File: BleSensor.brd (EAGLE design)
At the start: 31.7 x 37.3 mm, 13 parts, among them T1 BPW85C, U1 PIC12F1572/P

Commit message: Added sensors
Added sensors
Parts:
- added U2: LMT84-TO-92LP, Temperature sensor:TO92-LP
- moved T1 45.0 mm to (15.2, 27.3)
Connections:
- new net N$13: T1.A
- net GND: now also U2.2
- net RA3: now also U2.1
- net RA4: now also U2.3
- net RA5: no longer T1.A
- net VDD: no longer T1.K, U1.1
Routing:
- net VDD: track 80.4 -> 69.2 mm
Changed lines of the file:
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@@
 <?xml version="1.0" encoding="utf-8"?>
 <!DOCTYPE eagle SYSTEM "eagle.dtd">
-<eagle version="7.5.0">
+<eagle version="8.4.0">
 <drawing>
 <settings>
 <setting alwaysvectorfont="no"/>
+<setting keepoldvectorfont="yes"/>
 <setting verticaltext="up"/>
 </settings>
@@
 <layer number="51" name="tDocu" color="7" fill="1" visible="yes" active="yes"/>
 <layer number="52" name="bDocu" color="7" fill="1" visible="yes" active="yes"/>
+<layer number="88" name="SimResults" color="9" fill="1" visible="no" active="no"/>
+<layer number="89" name="SimProbes" color="9" fill="1" visible="no" active="no"/>
 <layer number="90" name="Modules" color="5" fill="1" visible="no" active="no"/>
 <layer number="91" name="Nets" color="2" fill="1" visible="no" active="no"/>
@@
 <param name="dpMaxLengthDifference" value="10mm"/>
 <param name="dpGapFactor" value="2.5"/>
-<param name="checkGrid" value="0"/>
-<param name="checkAngle" value="0"/>
 <param name="checkFont" value="1"/>
 <param name="checkRestrict" value="1"/>
+<param name="checkStop" value="0"/>
 <param name="useDiameter" value="13"/>
 <param name="maxErrors" value="50"/>
@@
 <element name="R2" library="resistor" package="M1206" value="47K" x="2.54" y="-3.81"/>
 <element name="R3" library="resistor" package="M1206" value="22K" x="2.54" y="-10.16"/>
-<element name="T1" library="Vishay_tsal4400_bpw85c" package="LED3MM" value="BPW85C" x="2.54" y="-15.875"/>
+<element name="T1" library="Vishay_tsal4400_bpw85c" package="LED3MM" value="BPW85C" x="15.24" y="27.305"/>
 <element name="C4" library="rcl" package="C1206" value="1nF" x="2.54" y="-21.59"/>
+<element name="U2" library="Temperature sensor" package="TO92-LP" value="LMT84-TO-92LP" x="3.175" y="-33.02"/>
 </elements>
 <signals>
@@
 <signal name="VDD">
 <contactref element="C1" pad="1"/>
-<contactref element="U1" pad="1"/>
 <contactref element="JP1" pad="10"/>
-<wire x1="3.81" y1="11.43" x2="12.7" y2="11.43" width="0.8128" layer="16"/>
 <contactref element="JP1" pad="9"/>
 <wire x1="3.81" y1="11.43" x2="3.81" y2="13.97" width="0.8128" layer="16"/>
@@
 <contactref element="C2" pad="1"/>
 <contactref element="C3" pad="1"/>
-<wire x1="12.7" y1="11.43" x2="12.7" y2="12.7" width="0.4064" layer="1"/>
 <wire x1="12.7" y1="12.7" x2="13.716" y2="13.716" width="0.4064" layer="1"/>
 <wire x1="13.716" y1="13.716" x2="15.11" y2="13.716" width="0.4064" layer="1"/>
@@
 <wire x1="16.51" y1="2.54" x2="16.51" y2="8.636" width="0.8128" layer="16"/>
 <wire x1="16.51" y1="8.636" x2="13.716" y2="11.43" width="0.8128" layer="16"/>
-<wire x1="13.716" y1="11.43" x2="12.7" y2="11.43" width="0.8128" layer="16"/>
 <wire x1="17.526" y1="1.524" x2="22.86" y2="1.524" width="0.8128" layer="16"/>
 <wire x1="22.86" y1="1.524" x2="24.13" y2="2.794" width="0.8128" layer="16"/>
@@
 <wire x1="23.876" y1="32.512" x2="21.458" y2="32.512" width="0.3048" layer="1"/>
 <wire x1="21.458" y1="32.512" x2="21.41" y2="32.56" width="0.4064" layer="1"/>
-<contactref element="T1" pad="K"/>
-<wire x1="3.81" y1="-15.875" x2="17.526" y2="1.524" width="0" layer="19" extent="16-16"/>
+<wire x1="13.716" y1="11.43" x2="12.7" y2="12.7" width="0" layer="19" extent="1-16"/>
+<wire x1="7.49" y1="11.43" x2="12.7" y2="12.7" width="0" layer="19" extent="1-1"/>
 </signal>
 <signal name="RA2">
@@
 <wire x1="22.86" y1="13.97" x2="25.4" y2="16.51" width="0.254" layer="1"/>
 <wire x1="25.4" y1="16.51" x2="26.67" y2="16.51" width="0.254" layer="1"/>
+<contactref element="U2" pad="3"/>
+<wire x1="12.7" y1="6.35" x2="4.445" y2="-31.75" width="0" layer="19" extent="1-1"/>
 </signal>
 <signal name="RA3">
@@
 <wire x1="4.064" y1="19.304" x2="3.81" y2="19.05" width="0.254" layer="1"/>
 <contactref element="R2" pad="2"/>
-<wire x1="17.526" y1="7.62" x2="4.826" y2="19.304" width="0" layer="19" extent="1-1"/>
-<wire x1="3.94" y1="-3.81" x2="12.7" y2="3.81" width="0" layer="19" extent="1-1"/>
+<contactref element="U2" pad="1"/>
+<wire x1="3.94" y1="-3.81" x2="1.905" y2="-31.75" width="0" layer="19" extent="1-1"/>
+<wire x1="12.7" y1="3.81" x2="3.94" y2="-3.81" width="0" layer="19" extent="1-1"/>
+<wire x1="4.826" y1="19.304" x2="17.526" y2="7.62" width="0" layer="19" extent="1-1"/>
 </signal>
 <signal name="RA5">
@@
 <wire x1="8.89" y1="10.16" x2="3.81" y2="8.89" width="0.254" layer="1"/>
 <wire x1="12.7" y1="8.89" x2="8.89" y2="10.16" width="0.254" layer="1"/>
-<contactref element="T1" pad="A"/>
 <contactref element="C4" pad="1"/>
-<wire x1="1.27" y1="-15.875" x2="1.14" y2="-21.59" width="0" layer="19" extent="1-1"/>
-<wire x1="8.89" y1="6.48" x2="1.27" y2="-15.875" width="0" layer="19" extent="1-1"/>
+<wire x1="8.89" y1="6.48" x2="1.14" y2="-21.59" width="0" layer="19" extent="1-1"/>
 <wire x1="8.89" y1="10.16" x2="8.89" y2="6.48" width="0" layer="19" extent="1-1"/>
 </signal>
@@
 <contactref element="R3" pad="1"/>
 <contactref element="C4" pad="2"/>
+<contactref element="U2" pad="2"/>
 <wire x1="15.872" y1="32.512" x2="21.41" y2="33.76" width="0" layer="19" extent="1-16"/>
 <wire x1="10.41" y1="33.76" x2="15.872" y2="32.512" width="0" layer="19" extent="1-16"/>
@@
 <wire x1="1.14" y1="-10.16" x2="8.89" y2="3.68" width="0" layer="19" extent="1-1"/>
 <wire x1="3.94" y1="-21.59" x2="1.14" y2="-10.16" width="0" layer="19" extent="1-1"/>
+<wire x1="3.175" y1="-31.75" x2="3.94" y2="-21.59" width="0" layer="19" extent="1-1"/>
 </signal>
 <signal name="BATT_MON">
@@
 <wire x1="3.94" y1="-10.16" x2="1.14" y2="-3.81" width="0" layer="19" extent="1-1"/>
 </signal>
+<signal name="N$13">
+<contactref element="T1" pad="A"/>
+</signal>
 </signals>

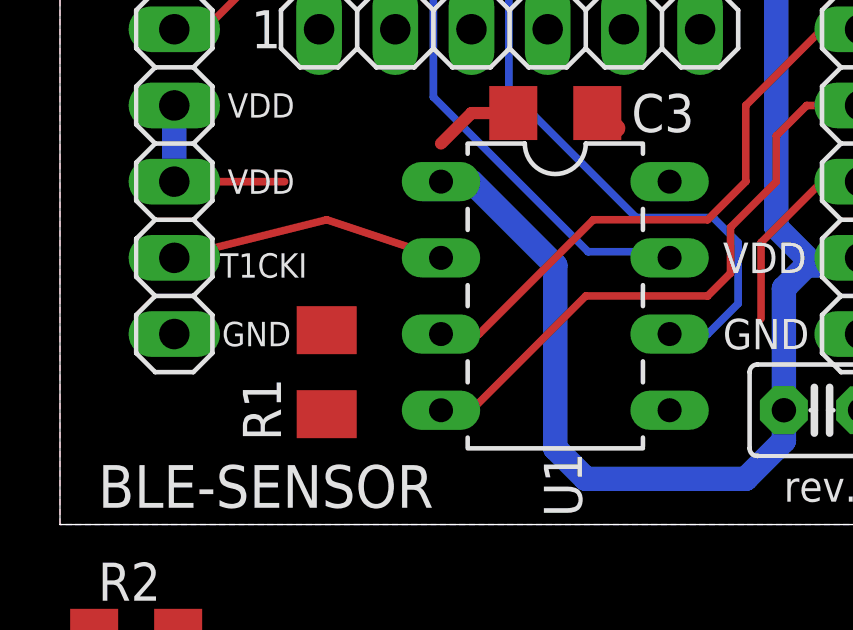
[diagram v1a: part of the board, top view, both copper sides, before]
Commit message: Fixed sensor inputs, added pdf Bitscope BLE Sensor pics
Fixed sensor inputs, added pdf Bitscope BLE Sensor pics
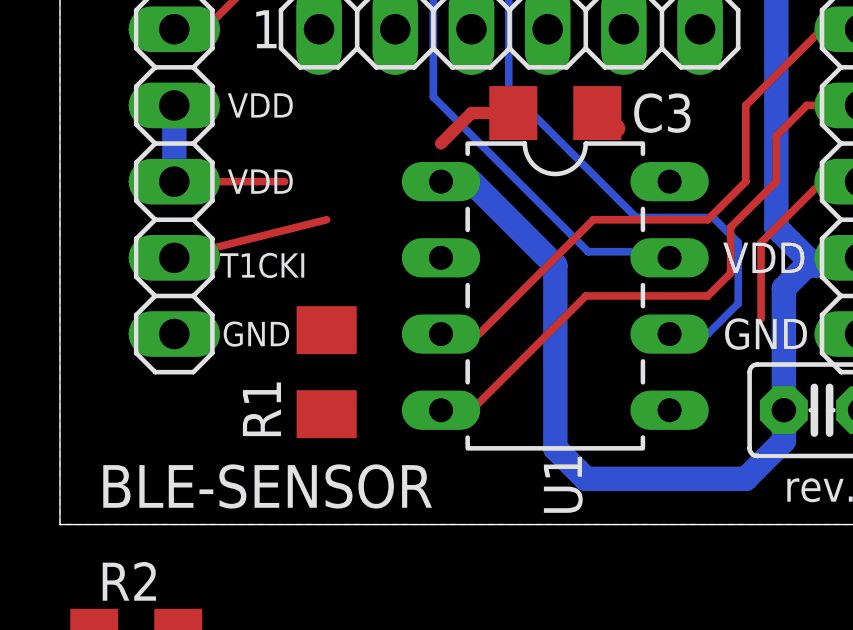
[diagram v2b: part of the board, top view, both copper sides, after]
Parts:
- C4: value 1nF -> 3n3
- R1: value 470K -> 100K
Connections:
- net N$13 renamed VE
- removed net N$12: JP1.4, U$1.P04
- new net TEMP: U2.3
- new net VC: T1.K
- new net WAKE-UP: R2.2, U2.1
- net BATT_MON: now also JP1.4, U$1.P04; no longer U1.5
- net RA2: now also JP1.7, U$1.P07, U1.5
- net RA3: no longer JP1.7, R2.2, U$1.P07, U2.1
- net RA4: no longer U2.3
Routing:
- net RA3: track 31.1 -> 18.9 mm
- net RA2: track 6.68 -> 17.8 mm
- net N$12: track 6.58 -> 0.00 mm
- net BATT_MON: track 0.00 -> 6.58 mm
- net RA5: track 9.25 -> 5.24 mm
- net RA4: track 19.7 -> 18.4 mm
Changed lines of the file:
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@@
 <?xml version="1.0" encoding="utf-8"?>
 <!DOCTYPE eagle SYSTEM "eagle.dtd">
-<eagle version="8.4.0">
+<eagle version="7.5.0">
 <drawing>
 <settings>
 <setting alwaysvectorfont="no"/>
-<setting keepoldvectorfont="yes"/>
 <setting verticaltext="up"/>
 </settings>
@@
 <param name="dpMaxLengthDifference" value="10mm"/>
 <param name="dpGapFactor" value="2.5"/>
+<param name="checkGrid" value="0"/>
+<param name="checkAngle" value="0"/>
 <param name="checkFont" value="1"/>
 <param name="checkRestrict" value="1"/>
-<param name="checkStop" value="0"/>
 <param name="useDiameter" value="13"/>
 <param name="maxErrors" value="50"/>
@@
 <attribute name="VALUE" x="7.366" y="13.335" size="1.27" layer="27"/>
 </element>
-<element name="R1" library="resistor" package="M1206" value="470K" x="8.89" y="5.08" smashed="yes" rot="R90">
+<element name="R1" library="resistor" package="M1206" value="100K" x="8.89" y="5.08" smashed="yes" rot="R90">
 <attribute name="NAME" x="7.366" y="2.794" size="1.27" layer="25" rot="R90"/>
 <attribute name="VALUE" x="11.43" y="3.81" size="1.27" layer="27" rot="R90"/>
@@
 <element name="R3" library="resistor" package="M1206" value="22K" x="2.54" y="-10.16"/>
 <element name="T1" library="Vishay_tsal4400_bpw85c" package="LED3MM" value="BPW85C" x="15.24" y="27.305"/>
-<element name="C4" library="rcl" package="C1206" value="1nF" x="2.54" y="-21.59"/>
+<element name="C4" library="rcl" package="C1206" value="3n3" x="2.54" y="-21.59"/>
 <element name="U2" library="Temperature sensor" package="TO92-LP" value="LMT84-TO-92LP" x="3.175" y="-33.02"/>
 </elements>
@@
 <contactref element="JP1" pad="3"/>
 <wire x1="3.81" y1="29.21" x2="5.2578" y2="29.21" width="0" layer="19" extent="1-1"/>
-</signal>
-<signal name="N$12">
-<contactref element="U$1" pad="P04"/>
-<wire x1="8.6868" y1="30.1244" x2="10.287" y2="30.1244" width="0.254" layer="1"/>
-<wire x1="5.2578" y1="26.6954" x2="8.6868" y2="30.1244" width="0.254" layer="1"/>
-<wire x1="10.287" y1="30.1244" x2="10.41" y2="30.16" width="0.254" layer="1"/>
-<contactref element="JP1" pad="4"/>
-<wire x1="3.81" y1="26.67" x2="5.2578" y2="26.6954" width="0" layer="19" extent="1-1"/>
 </signal>
 <signal name="5-TX">
@@
 </signal>
 <signal name="RA2">
+<contactref element="U$1" pad="P07"/>
+<contactref element="JP1" pad="7"/>
+<wire x1="10.41" y1="26.56" x2="10.41" y2="26.412" width="0.254" layer="1"/>
+<wire x1="10.41" y1="26.412" x2="9.648" y2="26.412" width="0.254" layer="1"/>
+<wire x1="9.648" y1="26.412" x2="7.62" y2="24.384" width="0.254" layer="1"/>
+<wire x1="7.62" y1="24.384" x2="7.62" y2="22.098" width="0.254" layer="1"/>
+<wire x1="7.62" y1="22.098" x2="4.826" y2="19.304" width="0.254" layer="1"/>
+<wire x1="4.826" y1="19.304" x2="4.064" y2="19.304" width="0.254" layer="1"/>
+<wire x1="4.064" y1="19.304" x2="3.81" y2="19.05" width="0.254" layer="1"/>
+<contactref element="U1" pad="5"/>
 <contactref element="JP2" pad="10"/>
 <wire x1="23.368" y1="6.858" x2="23.368" y2="9.398" width="0.254" layer="1"/>
 <wire x1="23.368" y1="9.398" x2="25.4" y2="11.43" width="0.254" layer="1"/>
 <wire x1="25.4" y1="11.43" x2="26.67" y2="11.43" width="0.254" layer="1"/>
+<wire x1="20.32" y1="3.81" x2="23.368" y2="6.858" width="0" layer="19" extent="1-1"/>
+<wire x1="7.62" y1="22.098" x2="23.368" y2="9.398" width="0" layer="19" extent="1-1"/>
 </signal>
 <signal name="6-RX">
@@
 </signal>
 <signal name="RA4">
-<contactref element="U1" pad="3"/>
-<wire x1="12.7" y1="6.35" x2="13.97" y2="6.35" width="0.254" layer="1"/>
 <wire x1="13.97" y1="6.35" x2="17.78" y2="10.16" width="0.254" layer="1"/>
 <wire x1="17.78" y1="10.16" x2="21.59" y2="10.16" width="0.254" layer="1"/>
@@
 <wire x1="22.86" y1="13.97" x2="25.4" y2="16.51" width="0.254" layer="1"/>
 <wire x1="25.4" y1="16.51" x2="26.67" y2="16.51" width="0.254" layer="1"/>
-<contactref element="U2" pad="3"/>
-<wire x1="12.7" y1="6.35" x2="4.445" y2="-31.75" width="0" layer="19" extent="1-1"/>
+<contactref element="U1" pad="3"/>
+<wire x1="12.7" y1="6.35" x2="13.97" y2="6.35" width="0" layer="19" extent="1-1"/>
 </signal>
 <signal name="RA3">
-<contactref element="U1" pad="4"/>
 <contactref element="JP2" pad="9"/>
-<wire x1="12.7" y1="3.81" x2="13.716" y2="3.81" width="0.254" layer="1"/>
 <wire x1="13.716" y1="3.81" x2="17.526" y2="7.62" width="0.254" layer="1"/>
 <wire x1="17.526" y1="7.62" x2="21.59" y2="7.62" width="0.254" layer="1"/>
@@
 <wire x1="23.876" y1="12.954" x2="24.892" y2="13.97" width="0.254" layer="1"/>
 <wire x1="24.892" y1="13.97" x2="26.67" y2="13.97" width="0.254" layer="1"/>
-<contactref element="U$1" pad="P07"/>
-<contactref element="JP1" pad="7"/>
-<wire x1="10.41" y1="26.56" x2="10.41" y2="26.412" width="0.254" layer="1"/>
-<wire x1="10.41" y1="26.412" x2="9.648" y2="26.412" width="0.254" layer="1"/>
-<wire x1="9.648" y1="26.412" x2="7.62" y2="24.384" width="0.254" layer="1"/>
-<wire x1="7.62" y1="24.384" x2="7.62" y2="22.098" width="0.254" layer="1"/>
-<wire x1="7.62" y1="22.098" x2="4.826" y2="19.304" width="0.254" layer="1"/>
-<wire x1="4.826" y1="19.304" x2="4.064" y2="19.304" width="0.254" layer="1"/>
-<wire x1="4.064" y1="19.304" x2="3.81" y2="19.05" width="0.254" layer="1"/>
-<contactref element="R2" pad="2"/>
-<contactref element="U2" pad="1"/>
-<wire x1="3.94" y1="-3.81" x2="1.905" y2="-31.75" width="0" layer="19" extent="1-1"/>
-<wire x1="12.7" y1="3.81" x2="3.94" y2="-3.81" width="0" layer="19" extent="1-1"/>
-<wire x1="4.826" y1="19.304" x2="17.526" y2="7.62" width="0" layer="19" extent="1-1"/>
-</signal>
-<signal name="RA5">
-<contactref element="JP1" pad="11"/>
-<contactref element="U1" pad="2"/>
-<contactref element="R1" pad="2"/>
-<wire x1="8.89" y1="10.16" x2="3.81" y2="8.89" width="0.254" layer="1"/>
-<wire x1="12.7" y1="8.89" x2="8.89" y2="10.16" width="0.254" layer="1"/>
-<contactref element="C4" pad="1"/>
-<wire x1="8.89" y1="6.48" x2="1.14" y2="-21.59" width="0" layer="19" extent="1-1"/>
-<wire x1="8.89" y1="10.16" x2="8.89" y2="6.48" width="0" layer="19" extent="1-1"/>
+<contactref element="U1" pad="4"/>
+<wire x1="12.7" y1="3.81" x2="13.716" y2="3.81" width="0" layer="19" extent="1-1"/>
 </signal>
 <signal name="N$1">
@@
 <wire x1="3.175" y1="-31.75" x2="3.94" y2="-21.59" width="0" layer="19" extent="1-1"/>
 </signal>
+<signal name="VE">
+<contactref element="T1" pad="A"/>
+</signal>
 <signal name="BATT_MON">
-<contactref element="U1" pad="5"/>
 <contactref element="R2" pad="1"/>
 <contactref element="R3" pad="2"/>
-<wire x1="1.14" y1="-3.81" x2="20.32" y2="3.81" width="0" layer="19" extent="1-1"/>
+<contactref element="U$1" pad="P04"/>
+<wire x1="8.6868" y1="30.1244" x2="10.287" y2="30.1244" width="0.254" layer="1"/>
+<wire x1="5.2578" y1="26.6954" x2="8.6868" y2="30.1244" width="0.254" layer="1"/>
+<wire x1="10.287" y1="30.1244" x2="10.41" y2="30.16" width="0.254" layer="1"/>
+<contactref element="JP1" pad="4"/>
+<wire x1="3.81" y1="26.67" x2="5.2578" y2="26.6954" width="0" layer="19" extent="1-1"/>
+<wire x1="1.14" y1="-3.81" x2="3.81" y2="26.67" width="0" layer="19" extent="1-1"/>
 <wire x1="3.94" y1="-10.16" x2="1.14" y2="-3.81" width="0" layer="19" extent="1-1"/>
 </signal>
-<signal name="N$13">
-<contactref element="T1" pad="A"/>
+<signal name="RA5">
+<contactref element="R1" pad="2"/>
+<contactref element="C4" pad="1"/>
+<contactref element="U1" pad="2"/>
+<contactref element="JP1" pad="11"/>
+<wire x1="8.89" y1="10.16" x2="3.81" y2="8.89" width="0.254" layer="1"/>
+<wire x1="8.89" y1="6.48" x2="1.14" y2="-21.59" width="0" layer="19" extent="1-1"/>
+<wire x1="8.89" y1="10.16" x2="8.89" y2="6.48" width="0" layer="19" extent="1-1"/>
+<wire x1="12.7" y1="8.89" x2="8.89" y2="10.16" width="0" layer="19" extent="1-1"/>
+</signal>
+<signal name="TEMP">
+<contactref element="U2" pad="3"/>
+</signal>
+<signal name="WAKE-UP">
+<contactref element="R2" pad="2"/>
+<contactref element="U2" pad="1"/>
+<wire x1="3.94" y1="-3.81" x2="1.905" y2="-31.75" width="0" layer="19" extent="1-1"/>
+</signal>
+<signal name="VC">
+<contactref element="T1" pad="K"/>
 </signal>
 </signals>
